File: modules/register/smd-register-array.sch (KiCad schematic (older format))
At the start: 36 parts, among them J1 Conn_01x32, U1 74HC08D,653, U2 74HC574PW,118, U3 74HC245D,653, U4 74HC245D,653, U5 74HC245D,653

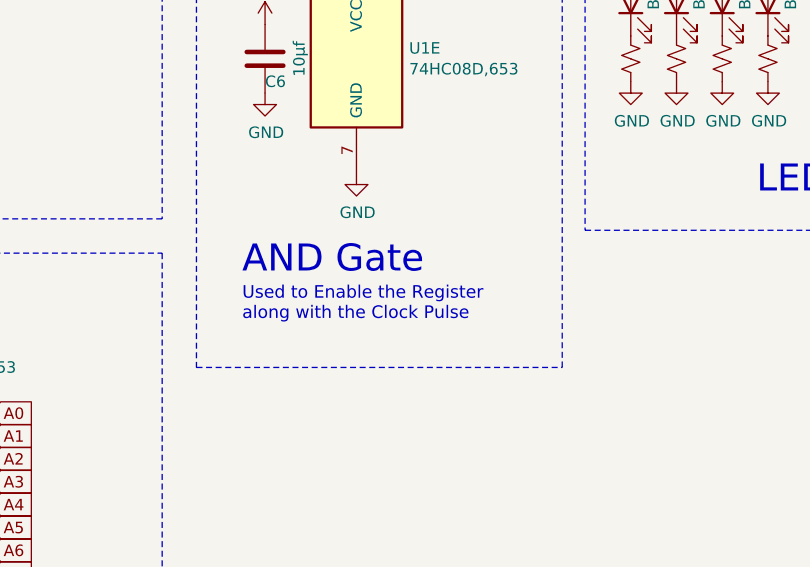
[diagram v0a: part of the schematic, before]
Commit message: Added SMD Modules
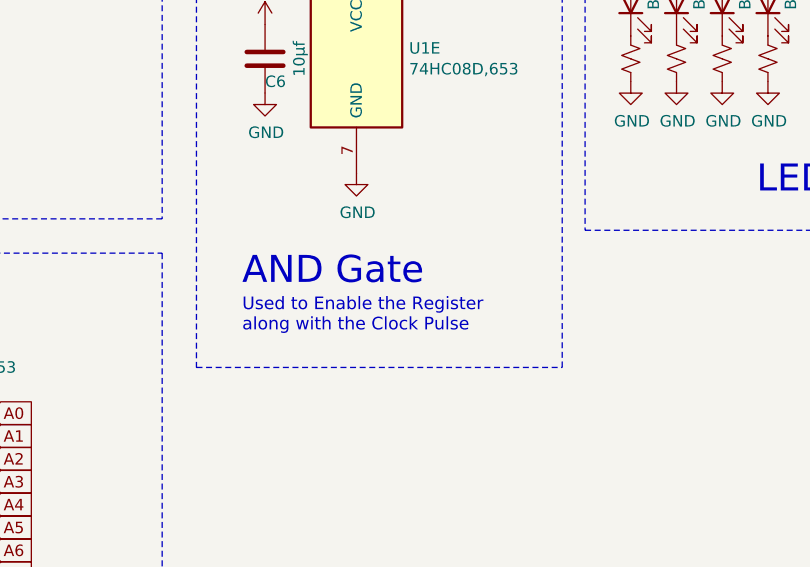
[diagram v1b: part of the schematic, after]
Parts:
- C1, C2, C3, C4, C6: JCLC (none) -> C15525
- C5: JCLC (none) -> C140924
- D1, D2, D3, D4, D5, D6, D7, D8: JCLC (none) -> C72043
- D10, D11, D12, D9: JCLC (none) -> C72041
- R1, R10, R11, R12, R2, R3, R4, R5, R6, R7, R8, R9: JCLC (none) -> C11702
- U2: JCLC (none) -> C93762
- U3, U4, U5: JCLC (none) -> C5625
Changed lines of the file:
@@
 F 4 "C5625" H 5300 2350 50  0001 C CNN "JLCPCB"
 F 5 "Transceiver, Non-Inverting 3-State Outputs SOIC-20_300mil 74 Series ROHS" H 5300 2350 50  0001 C CNN "Description"
+F 6 "C5625" H 5300 2350 50  0001 C CNN "JCLC"
 	1    5300 2350
 	1    0    0    -1
@@
 F 4 "C72043" V 9500 3100 50  0001 C CNN "JLCPCB"
 F 5 "GRN" H 9600 3000 50  0000 R CNN "Color"
+F 6 "C72043" H 9500 3100 50  0001 C CNN "JCLC"
 	1    9500 3100
 	0    -1   -1   0
@@
 F 4 "±1% 1/16W ±100ppm/℃ 1kΩ 0402 Chip Resistor - Surface Mount ROHS" H 9500 3350 50  0001 C CNN "Description"
 F 5 "C11702" H 9500 3350 50  0001 C CNN "JLCPCB"
+F 6 "C11702" H 9500 3350 50  0001 C CNN "JCLC"
 	1    9500 3350
 	1    0    0    -1
@@
 F 4 "C93762" H 2700 2300 50  0001 C CNN "JLCPCB"
 F 5 "D Type 74HC Tri-State,Non-Inverted TSSOP-20 Flip Flops ROHS" H 2700 2300 50  0001 C CNN "Description"
+F 6 "C93762" H 2700 2300 50  0001 C CNN "JCLC"
 	1    2700 2300
 	1    0    0    -1
@@
 F 4 "C72043" V 9700 3100 50  0001 C CNN "JLCPCB"
 F 5 "GRN" H 9800 3000 50  0000 R CNN "Color"
+F 6 "C72043" H 9700 3100 50  0001 C CNN "JCLC"
 	1    9700 3100
 	0    -1   -1   0
@@
 F 4 "±1% 1/16W ±100ppm/℃ 1kΩ 0402 Chip Resistor - Surface Mount ROHS" H 9700 3350 50  0001 C CNN "Description"
 F 5 "C11702" H 9700 3350 50  0001 C CNN "JLCPCB"
+F 6 "C11702" H 9700 3350 50  0001 C CNN "JCLC"
 	1    9700 3350
 	1    0    0    -1
@@
 F 4 "C72043" V 9900 3100 50  0001 C CNN "JLCPCB"
 F 5 "GRN" H 10000 3000 50  0000 R CNN "Color"
+F 6 "C72043" H 9900 3100 50  0001 C CNN "JCLC"
 	1    9900 3100
 	0    -1   -1   0
@@
 F 4 "±1% 1/16W ±100ppm/℃ 1kΩ 0402 Chip Resistor - Surface Mount ROHS" H 9900 3350 50  0001 C CNN "Description"
 F 5 "C11702" H 9900 3350 50  0001 C CNN "JLCPCB"
+F 6 "C11702" H 9900 3350 50  0001 C CNN "JCLC"
 	1    9900 3350
 	1    0    0    -1
@@
 F 4 "C72043" V 10100 3100 50  0001 C CNN "JLCPCB"
 F 5 "GRN" H 10200 3000 50  0000 R CNN "Color"
+F 6 "C72043" H 10100 3100 50  0001 C CNN "JCLC"
 	1    10100 3100
 	0    -1   -1   0
@@
 F 4 "±1% 1/16W ±100ppm/℃ 1kΩ 0402 Chip Resistor - Surface Mount ROHS" H 10100 3350 50  0001 C CNN "Description"
 F 5 "C11702" H 10100 3350 50  0001 C CNN "JLCPCB"
+F 6 "C11702" H 10100 3350 50  0001 C CNN "JCLC"
 	1    10100 3350
 	1    0    0    -1
@@
 F 4 "C72043" V 10300 3100 50  0001 C CNN "JLCPCB"
 F 5 "GRN" H 10400 3000 50  0000 R CNN "Color"
+F 6 "C72043" H 10300 3100 50  0001 C CNN "JCLC"
 	1    10300 3100
 	0    -1   -1   0
@@
 F 4 "±1% 1/16W ±100ppm/℃ 1kΩ 0402 Chip Resistor - Surface Mount ROHS" H 10300 3350 50  0001 C CNN "Description"
 F 5 "C11702" H 10300 3350 50  0001 C CNN "JLCPCB"
+F 6 "C11702" H 10300 3350 50  0001 C CNN "JCLC"
 	1    10300 3350
 	1    0    0    -1
@@
 F 4 "C72043" V 10500 3100 50  0001 C CNN "JLCPCB"
 F 5 "GRN" H 10600 3000 50  0000 R CNN "Color"
+F 6 "C72043" H 10500 3100 50  0001 C CNN "JCLC"
 	1    10500 3100
 	0    -1   -1   0
@@
 F 4 "±1% 1/16W ±100ppm/℃ 1kΩ 0402 Chip Resistor - Surface Mount ROHS" H 10500 3350 50  0001 C CNN "Description"
 F 5 "C11702" H 10500 3350 50  0001 C CNN "JLCPCB"
+F 6 "C11702" H 10500 3350 50  0001 C CNN "JCLC"
 	1    10500 3350
 	1    0    0    -1
@@
 F 4 "C72043" V 10700 3100 50  0001 C CNN "JLCPCB"
 F 5 "GRN" H 10800 3000 50  0000 R CNN "Color"
+F 6 "C72043" H 10700 3100 50  0001 C CNN "JCLC"
 	1    10700 3100
 	0    -1   -1   0
@@
 F 4 "±1% 1/16W ±100ppm/℃ 1kΩ 0402 Chip Resistor - Surface Mount ROHS" H 10700 3350 50  0001 C CNN "Description"
 F 5 "C11702" H 10700 3350 50  0001 C CNN "JLCPCB"
+F 6 "C11702" H 10700 3350 50  0001 C CNN "JCLC"
 	1    10700 3350
 	1    0    0    -1
@@
 F 4 "C72043" V 10900 3100 50  0001 C CNN "JLCPCB"
 F 5 "GRN" H 11000 3000 50  0000 R CNN "Color"
+F 6 "C72043" H 10900 3100 50  0001 C CNN "JCLC"
 	1    10900 3100
 	0    -1   -1   0
@@
 F 4 "±1% 1/16W ±100ppm/℃ 1kΩ 0402 Chip Resistor - Surface Mount ROHS" H 10900 3350 50  0001 C CNN "Description"
 F 5 "C11702" H 10900 3350 50  0001 C CNN "JLCPCB"
+F 6 "C11702" H 10900 3350 50  0001 C CNN "JCLC"
 	1    10900 3350
 	1    0    0    -1
@@
 F 5 "X5R 6.3V ±20% 10uF 0402 Multilayer Ceramic Capacitors MLCC - SMD/SMT ROHS" H 1500 1850 50  0001 C CNN "Description"
 F 6 "10µf" V 1650 1850 50  0000 C CNN "C"
+F 7 "C15525" H 1500 1850 50  0001 C CNN "JCLC"
 	1    1500 1850
 	1    0    0    -1
@@
 F 5 "X5R 6.3V ±20% 10uF 0402 Multilayer Ceramic Capacitors MLCC - SMD/SMT ROHS" H 4100 2300 50  0001 C CNN "Description"
 F 6 "10µf" V 4250 2300 50  0000 C CNN "C"
+F 7 "C15525" H 4100 2300 50  0001 C CNN "JCLC"
 	1    4100 2300
 	1    0    0    -1
@@
 F 5 "X5R 6.3V ±20% 10uF 0402 Multilayer Ceramic Capacitors MLCC - SMD/SMT ROHS" H 1250 5250 50  0001 C CNN "Description"
 F 6 "10µf" V 1400 5250 50  0000 C CNN "C"
+F 7 "C15525" H 1250 5250 50  0001 C CNN "JCLC"
 	1    1250 5250
 	1    0    0    -1
@@
 F 5 "C140924" H 10150 1650 50  0001 C CNN "JLCPCB"
 F 6 "- - 5mm 100uF 10V -45℃~+105℃ ±20% 5.8mm 2000hrs 105℃ SMD,5x5.8mm Aluminum Electrolytic Capacitors - SMD ROHS" H 10150 1650 50  0001 C CNN "Description"
+F 7 "C140924" H 10150 1650 50  0001 C CNN "JCLC"
 	1    10150 1650
 	1    0    0    -1
@@
 F 5 "X5R 6.3V ±20% 10uF 0402 Multilayer Ceramic Capacitors MLCC - SMD/SMT ROHS" H 4100 5300 50  0001 C CNN "Description"
 F 6 "10µf" V 4250 5300 50  0000 C CNN "C"
+F 7 "C15525" H 4100 5300 50  0001 C CNN "JCLC"
 	1    4100 5300
 	1    0    0    -1
@@
 F 4 "±1% 1/16W ±100ppm/℃ 1kΩ 0402 Chip Resistor - Surface Mount ROHS" H 9100 3350 50  0001 C CNN "Description"
 F 5 "C11702" H 9100 3350 50  0001 C CNN "JLCPCB"
+F 6 "C11702" H 9100 3350 50  0001 C CNN "JCLC"
 	1    9100 3350
 	1    0    0    -1
@@
 F 4 "±1% 1/16W ±100ppm/℃ 1kΩ 0402 Chip Resistor - Surface Mount ROHS" H 8900 3350 50  0001 C CNN "Description"
 F 5 "C11702" H 8900 3350 50  0001 C CNN "JLCPCB"
+F 6 "C11702" H 8900 3350 50  0001 C CNN "JCLC"
 	1    8900 3350
 	1    0    0    -1
@@
 F 4 "±1% 1/16W ±100ppm/℃ 1kΩ 0402 Chip Resistor - Surface Mount ROHS" H 8700 3350 50  0001 C CNN "Description"
 F 5 "C11702" H 8700 3350 50  0001 C CNN "JLCPCB"
+F 6 "C11702" H 8700 3350 50  0001 C CNN "JCLC"
 	1    8700 3350
 	1    0    0    -1
@@
 F 4 "±1% 1/16W ±100ppm/℃ 1kΩ 0402 Chip Resistor - Surface Mount ROHS" H 8500 3350 50  0001 C CNN "Description"
 F 5 "C11702" H 8500 3350 50  0001 C CNN "JLCPCB"
+F 6 "C11702" H 8500 3350 50  0001 C CNN "JCLC"
 	1    8500 3350
 	1    0    0    -1
@@
 F 4 "C72041" V 8500 3100 50  0001 C CNN "JLCPCB"
 F 5 "BLU" H 8600 3000 50  0000 R CNN "Color"
+F 6 "C72041" H 8500 3100 50  0001 C CNN "JCLC"
 	1    8500 3100
 	0    -1   -1   0
@@
 F 4 "C72041" V 8700 3100 50  0001 C CNN "JLCPCB"
 F 5 "BLU" H 8800 3000 50  0000 R CNN "Color"
+F 6 "C72041" H 8700 3100 50  0001 C CNN "JCLC"
 	1    8700 3100
 	0    -1   -1   0
@@
 F 4 "C72041" V 8900 3100 50  0001 C CNN "JLCPCB"
 F 5 "BLU" H 9000 3000 50  0000 R CNN "Color"
+F 6 "C72041" H 8900 3100 50  0001 C CNN "JCLC"
 	1    8900 3100
 	0    -1   -1   0
@@
 F 4 "C72041" V 9100 3100 50  0001 C CNN "JLCPCB"
 F 5 "BLU" H 9200 3000 50  0000 R CNN "Color"
+F 6 "C72041" H 9100 3100 50  0001 C CNN "JCLC"
 	1    9100 3100
 	0    -1   -1   0
@@
 F 4 "C5625" H 2400 5400 50  0001 C CNN "JLCPCB"
 F 5 "Transceiver, Non-Inverting 3-State Outputs SOIC-20_300mil 74 Series ROHS" H 2400 5400 50  0001 C CNN "Description"
+F 6 "C5625" H 2400 5400 50  0001 C CNN "JCLC"
 	1    2400 5400
 	1    0    0    -1
@@
 F 4 "C5625" H 5200 5400 50  0001 C CNN "JLCPCB"
 F 5 "Transceiver, Non-Inverting 3-State Outputs SOIC-20_300mil 74 Series ROHS" H 5200 5400 50  0001 C CNN "Description"
+F 6 "C5625" H 5200 5400 50  0001 C CNN "JCLC"
 	1    5200 5400
 	1    0    0    -1
@@
 F 5 "X5R 6.3V ±20% 10uF 0402 Multilayer Ceramic Capacitors MLCC - SMD/SMT ROHS" H 6900 3350 50  0001 C CNN "Description"
 F 6 "10µf" V 7050 3350 50  0000 C CNN "C"
+F 7 "C15525" H 6900 3350 50  0001 C CNN "JCLC"
 	1    6900 3350
 	1    0    0    -1
@@
 Wire Notes Line
 	10550 2300 10550 1100
-Text Notes 6800 4300 0    118  ~ 0
+Text Notes 6800 4350 0    118  ~ 0
 AND Gate
-Text Notes 6800 4500 0    55   ~ 0
+Text Notes 6800 4550 0    55   ~ 0
 Used to Enable the Register\nalong with the Clock Pulse
 Wire Notes Line
